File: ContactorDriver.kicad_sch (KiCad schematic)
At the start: 24 parts, among them Con1 LED, Con2 LED, J10 Conn_01x04, J11 Conn_01x04, Q2 IRLML0030, Q3 IRLML0030, U5 TCMT1106, U6 TCMT1106

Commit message: replaced 0805 with 0603, changed logic analyzer symbol and silkscreen
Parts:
- C14, C15, C16, C17: footprint Capacitor_SMD:C_0805_2012Metric -> Capacitor_SMD:C_0603_1608Metric
- Con1, Con2: footprint LED_SMD:LED_0805_2012Metric -> LED_SMD:LED_0603_1608Metric
- R12, R13, R14, R15, R16, R17, R18, R19, R20, R21: footprint Resistor_SMD:R_0805_2012Metric -> Resistor_SMD:R_0603_1608Metric
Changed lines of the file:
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@@
 			)
 		)
-		(property "Footprint" "Resistor_SMD:R_0805_2012Metric"
+		(property "Footprint" "Resistor_SMD:R_0603_1608Metric"
 			(at 98.171 107.061 90)
 			(effects
@@
 			)
 		)
-		(property "Footprint" "Resistor_SMD:R_0805_2012Metric"
+		(property "Footprint" "Resistor_SMD:R_0603_1608Metric"
 			(at 69.596 118.999 90)
 			(effects
@@
 			)
 		)
-		(property "Footprint" "Resistor_SMD:R_0805_2012Metric"
+		(property "Footprint" "Resistor_SMD:R_0603_1608Metric"
 			(at 100.711 70.739 90)
 			(effects
@@
 			)
 		)
-		(property "Footprint" "Capacitor_SMD:C_0805_2012Metric"
+		(property "Footprint" "Capacitor_SMD:C_0603_1608Metric"
 			(at 63.1952 114.935 0)
 			(effects
@@
 			)
 		)
-		(property "Footprint" "Resistor_SMD:R_0805_2012Metric"
+		(property "Footprint" "Resistor_SMD:R_0603_1608Metric"
 			(at 225.679 38.354 90)
 			(effects
@@
 			)
 		)
-		(property "Footprint" "Resistor_SMD:R_0805_2012Metric"
+		(property "Footprint" "Resistor_SMD:R_0603_1608Metric"
 			(at 190.246 119.634 90)
 			(effects
@@
 			)
 		)
-		(property "Footprint" "Capacitor_SMD:C_0805_2012Metric"
+		(property "Footprint" "Capacitor_SMD:C_0603_1608Metric"
 			(at 183.8452 115.57 0)
 			(effects
@@
 			)
 		)
-		(property "Footprint" "Resistor_SMD:R_0805_2012Metric"
+		(property "Footprint" "Resistor_SMD:R_0603_1608Metric"
 			(at 218.186 107.696 90)
 			(effects
@@
 			)
 		)
-		(property "Footprint" "LED_SMD:LED_0805_2012Metric"
+		(property "Footprint" "LED_SMD:LED_0603_1608Metric"
 			(at 217.805 45.72 0)
 			(effects
@@
 			)
 		)
-		(property "Footprint" "Capacitor_SMD:C_0805_2012Metric"
+		(property "Footprint" "Capacitor_SMD:C_0603_1608Metric"
 			(at 101.9048 116.205 0)
 			(effects
@@
 			)
 		)
-		(property "Footprint" "Resistor_SMD:R_0805_2012Metric"
+		(property "Footprint" "Resistor_SMD:R_0603_1608Metric"
 			(at 103.759 37.719 90)
 			(effects
@@
 			)
 		)
-		(property "Footprint" "Resistor_SMD:R_0805_2012Metric"
+		(property "Footprint" "Resistor_SMD:R_0603_1608Metric"
 			(at 222.631 71.374 90)
 			(effects
@@
 			)
 		)
-		(property "Footprint" "Resistor_SMD:R_0805_2012Metric"
+		(property "Footprint" "Resistor_SMD:R_0603_1608Metric"
 			(at 194.564 110.744 90)
 			(effects
@@
 			)
 		)
-		(property "Footprint" "LED_SMD:LED_0805_2012Metric"
+		(property "Footprint" "LED_SMD:LED_0603_1608Metric"
 			(at 95.885 45.085 0)
 			(effects
@@
 			)
 		)
-		(property "Footprint" "Resistor_SMD:R_0805_2012Metric"
+		(property "Footprint" "Resistor_SMD:R_0603_1608Metric"
 			(at 73.914 110.109 90)
 			(effects
@@
 			)
 		)
-		(property "Footprint" "Capacitor_SMD:C_0805_2012Metric"
+		(property "Footprint" "Capacitor_SMD:C_0603_1608Metric"
 			(at 221.9198 118.11 0)
 			(effects

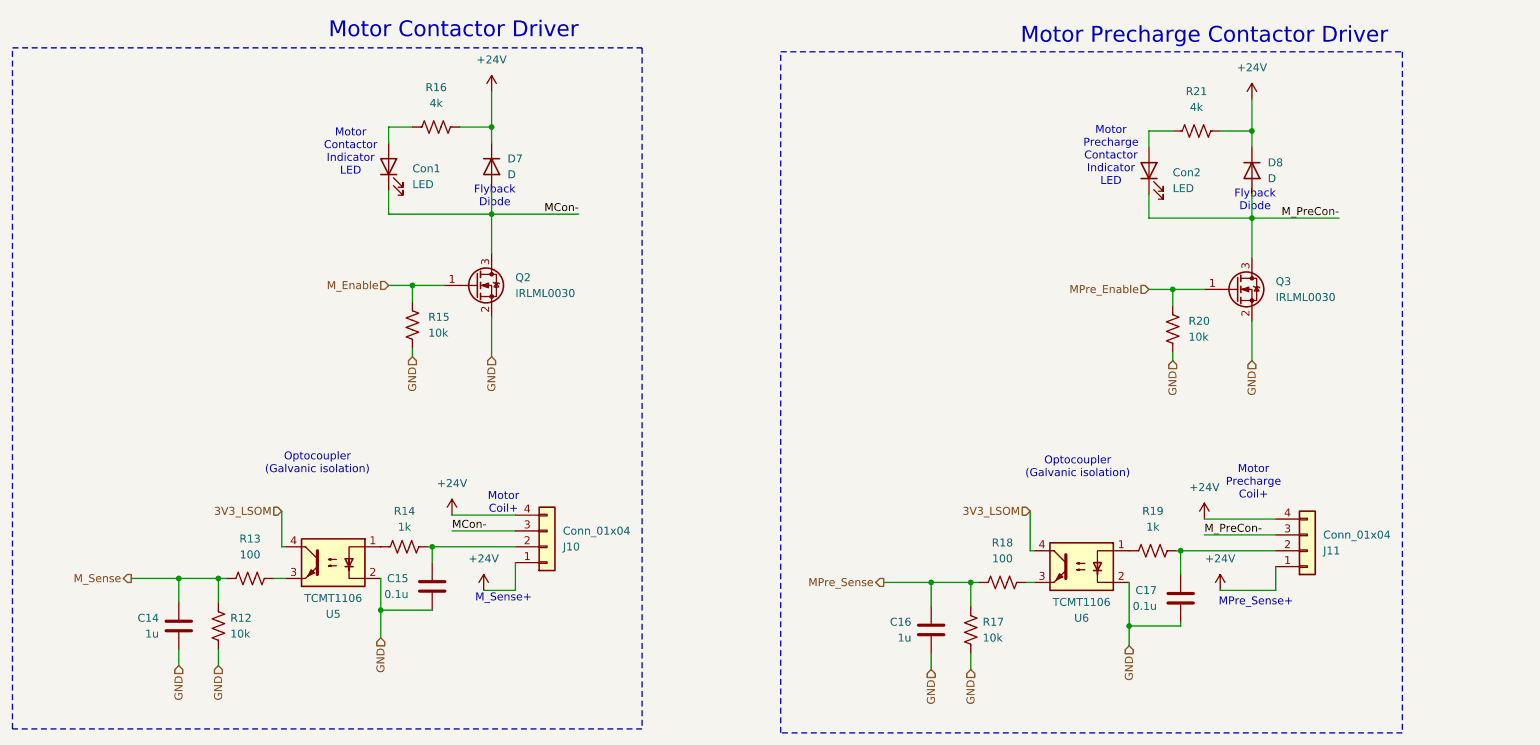
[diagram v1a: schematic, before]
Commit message: changed rpp ic
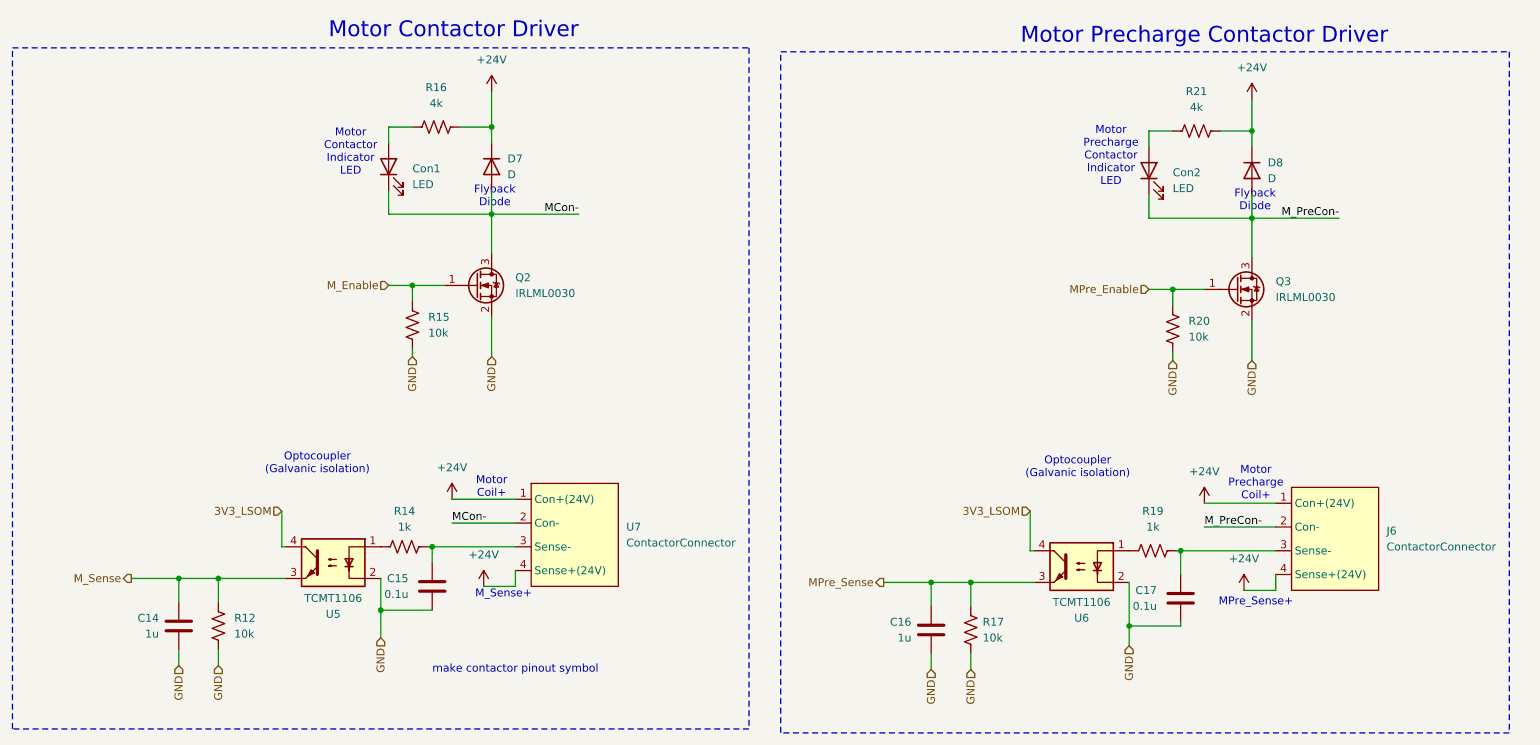
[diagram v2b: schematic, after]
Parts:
- removed J10, J11: Conn_01x04, UTSVT_Connectors:Molex_Nano-Fit_105309-xx04_1x04_P2.50mm_Vertical, symbol Connector_Generic:Conn_01x04
- removed R13, R18: 100, Resistor_SMD:R_0603_1608Metric, symbol Device:R_US
- added J6, U7: ContactorConnector, symbol UTSVT_Connectors:ContactorConnector
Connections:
- net +24V: now also J6.1 (Con+(24V)), J6.4 (Sense+(24V)), U7.1 (Con+(24V)), U7.4 (Sense+(24V))
- net MCon-: now also U7.2 (Con-)
- net MPre_Sense: now also U6.3
- net M_PreCon-: now also J6.2 (Con-)
- net M_Sense: now also U5.3
- net at C15.1, R14.1: now also U7.3 (Sense-)
- net at C17.1, R19.1: now also J6.3 (Sense-)
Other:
- note added: "make contactor pinout symbol"

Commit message: as;ldfkjasdl;f
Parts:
- removed U7: ContactorConnector, symbol UTSVT_Connectors:ContactorConnector
- added J7: ContactorConnector, UTSVT_Connectors:Molex_Nano-Fit_105309-xx04_1x04_P2.50mm_Vertical, symbol UTSVT_Connectors:ContactorConnector
- J6: footprint (none) -> UTSVT_Connectors:Molex_Nano-Fit_105309-xx04_1x04_P2.50mm_Vertical
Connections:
- net +24V: now also J7.1 (Con+(24V)), J7.4 (Sense+(24V))
- net MCon-: now also J7.2 (Con-)
- net at C15.1, R14.1: now also J7.3 (Sense-)
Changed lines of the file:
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@@
 			)
 		)
-		(property "Footprint" ""
+		(property "Footprint" "UTSVT_Connectors:Molex_Nano-Fit_105309-xx04_1x04_P2.50mm_Vertical"
 			(at 243.205 95.25 0)
 			(effects
@@
 				(path "/795c8e51-3ded-4d21-b864-aaff31c5def7/838dfc75-afcf-4845-8c43-fcef4e0ee00c"
 					(reference "R15")
+					(unit 1)
+				)
+			)
+		)
+	)
+	(symbol
+		(lib_id "UTSVT_Connectors:ContactorConnector")
+		(at 121.285 94.615 0)
+		(unit 1)
+		(exclude_from_sim no)
+		(in_bom yes)
+		(on_board yes)
+		(dnp no)
+		(fields_autoplaced yes)
+		(property "Reference" "J7"
+			(at 133.985 102.8699 0)
+			(effects
+				(font
+					(size 1.27 1.27)
+				)
+				(justify left)
+			)
+		)
+		(property "Value" "ContactorConnector"
+			(at 133.985 105.4099 0)
+			(effects
+				(font
+					(size 1.27 1.27)
+				)
+				(justify left)
+			)
+		)
+		(property "Footprint" "UTSVT_Connectors:Molex_Nano-Fit_105309-xx04_1x04_P2.50mm_Vertical"
+			(at 121.285 94.615 0)
+			(effects
+				(font
+					(size 1.27 1.27)
+				)
+				(hide yes)
+			)
+		)
+		(property "Datasheet" ""
+			(at 121.285 94.615 0)
+			(effects
+				(font
+					(size 1.27 1.27)
+				)
+				(hide yes)
+			)
+		)
+		(property "Description" "Pinout for contactor connectors."
+			(at 122.555 104.013 0)
+			(effects
+				(font
+					(size 1.27 1.27)
+				)
+				(hide yes)
+			)
+		)
+		(pin "2"
+		)
+		(pin "3"
+		)
+		(pin "4"
+		)
+		(pin "1"
+		)
+		(instances
+			(project "VehicleControlUnit"
+				(path "/795c8e51-3ded-4d21-b864-aaff31c5def7/838dfc75-afcf-4845-8c43-fcef4e0ee00c"
+					(reference "J7")
 					(unit 1)
 				)
@@
 					(unit 1)
 				)
-			)
-		)
-	)
-	(symbol
-		(lib_id "UTSVT_Connectors:ContactorConnector")
-		(at 121.285 94.615 0)
-		(unit 1)
-		(exclude_from_sim no)
-		(in_bom yes)
-		(on_board yes)
-		(dnp no)
-		(fields_autoplaced yes)
-		(property "Reference" "U7"
-			(at 133.985 102.8699 0)
-			(effects
-				(font
-					(size 1.27 1.27)
-				)
-				(justify left)
-			)
-		)
-		(property "Value" "ContactorConnector"
-			(at 133.985 105.4099 0)
-			(effects
-				(font
-					(size 1.27 1.27)
-				)
-				(justify left)
-			)
-		)
-		(property "Footprint" ""
-			(at 121.285 94.615 0)
-			(effects
-				(font
-					(size 1.27 1.27)
-				)
-				(hide yes)
-			)
-		)
-		(property "Datasheet" ""
-			(at 121.285 94.615 0)
-			(effects
-				(font
-					(size 1.27 1.27)
-				)
-				(hide yes)
-			)
-		)
-		(property "Description" "Pinout for contactor connectors."
-			(at 122.555 104.013 0)
-			(effects
-				(font
-					(size 1.27 1.27)
-				)
-				(hide yes)
-			)
-		)
-		(pin "3"
-		)
-		(pin "4"
-		)
-		(pin "1"
-		)
-		(pin "2"
-		)
-		(instances
-			(project ""
-				(path "/795c8e51-3ded-4d21-b864-aaff31c5def7/838dfc75-afcf-4845-8c43-fcef4e0ee00c"
-					(reference "U7")
-					(unit 1)
-				)

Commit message: lakshay edits
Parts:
- removed U5, U6: TCMT1106, Package_SO:SOP-4_4.4x2.6mm_P1.27mm, symbol Isolator:TCMT1106
- added U2, U3: EL3H7, UTSVT_ICs:EL3H7, symbol UTSVT_ICs:EL3H7
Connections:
- net 3V3_LSOM: now also U2.4, U3.4
- net GND: now also C15.1, C17.1, U2.2, U3.2; no longer C15.2, C17.2
- net MPre_Sense: now also U2.3
- net M_Sense: now also U3.3
- net at J6.3 (Sense-), R19.1: no longer C17.1
- net at J7.3 (Sense-), R14.1: no longer C15.1
- net at R14.2: now also C15.2, U3.1
- net at R19.2: now also C17.2, U2.1
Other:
- moved on the sheet: C15, C17, R14, R19

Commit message: ravi's bs
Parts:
- R16, R21: value 4k -> 4.3k
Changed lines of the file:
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@@
 			)
 		)
-		(property "Value" "4k"
+		(property "Value" "4.3k"
 			(at 225.425 35.56 90)
 			(effects
@@
 		(fields_autoplaced yes)
 		(property "Reference" "R16"
-			(at 103.505 32.385 90)
-			(effects
-				(font
-					(size 1.27 1.27)
-				)
-			)
-		)
-		(property "Value" "4k"
-			(at 103.505 34.925 90)
-			(effects
-				(font
+			(at 103.505 33.02 90)
+			(effects
+				(font
+					(size 1.27 1.27)
+				)
+			)
+		)
+		(property "Value" "4.3k"
+			(at 103.505 35.56 90)
+			(effects
+				(font

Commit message: start of RevB. BOM for revA
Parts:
- C14, C16: Mouser Part Number (none) -> 963-UMK107BJ105KA-T; P/N (none) -> UMK107BJ105KA-T
- C15, C17: Mouser Part Number (none) -> 963-HMK107B7104KA-T; P/N (none) -> HMK107B7104KA-T
- Con1, Con2, D7, D8: P/N (none) -> XL-1608UBC-06A
- J6, J7: Mouser Part Number (none) -> 538-105309-1104; P/N (none) -> 105309-1104
- Q2, Q3: Mouser Part Number (none) -> 942-IRLML0030TRPBF; P/N (none) -> IRLML0030TRPBF
- R12, R15, R17, R20: Mouser Part Number (none) -> 71-CRCW060310K0FKEI; P/N (none) -> CRCW060310K0FKEI
- R14, R19: Mouser Part Number (none) -> 71-CRCW06031K00FKEI; P/N (none) -> CRCW06031K00FKEI
- R16, R21: Mouser Part Number (none) -> 71-CRCW0603-4.3K-E3; P/N (none) -> CRCW06034K30FKEA
- U2, U3: Mouser Part Number (none) -> 638-EL3H7DTAVG

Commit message: workday
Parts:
- removed J6, J7: ContactorConnector, UTSVT_Connectors:Molex_Nano-Fit_105309-xx04_1x04_P2.50mm_Vertical, symbol UTSVT_Connectors:ContactorConnector
- C14, C15, C16, C17: footprint Capacitor_SMD:C_0603_1608Metric -> Capacitor_SMD:C_0603_1608Metric_Pad1.08x0.95mm_HandSolder
- R12, R14, R15, R16, R17, R19, R20, R21: footprint Resistor_SMD:R_0603_1608Metric -> Resistor_SMD:R_0603_1608Metric_Pad0.98x0.95mm_HandSolder
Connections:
- net MPre_Sense-: now reaches R19.1
- net M_Sense-: now reaches R14.1
- net M_PreCon- renamed MPreCon-
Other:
- note removed: "Motor Precharge Coil+"
- note removed: "make contactor pinout symbol"
- moved on the sheet: C14, C15, Con1, D7, Q2, R12, R14, R15, R16, U3

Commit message: rev B
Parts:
- Con1, Con2: footprint LED_SMD:LED_0603_1608Metric -> LED_SMD:LED_0603_1608Metric_Pad1.05x0.95mm_HandSolder
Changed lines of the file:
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@@
 			)
 		)
-		(property "Footprint" "LED_SMD:LED_0603_1608Metric"
+		(property "Footprint" "LED_SMD:LED_0603_1608Metric_Pad1.05x0.95mm_HandSolder"
 			(at 217.805 45.72 0)
 			(effects
@@
 			)
 		)
-		(property "Footprint" "LED_SMD:LED_0603_1608Metric"
+		(property "Footprint" "LED_SMD:LED_0603_1608Metric_Pad1.05x0.95mm_HandSolder"
 			(at 96.52 45.72 0)
 			(effects
